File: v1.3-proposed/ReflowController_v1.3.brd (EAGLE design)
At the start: 95.2 x 50.8 mm, 53 parts, among them J1 AVR_SPI_PRG_62X3_LOCK

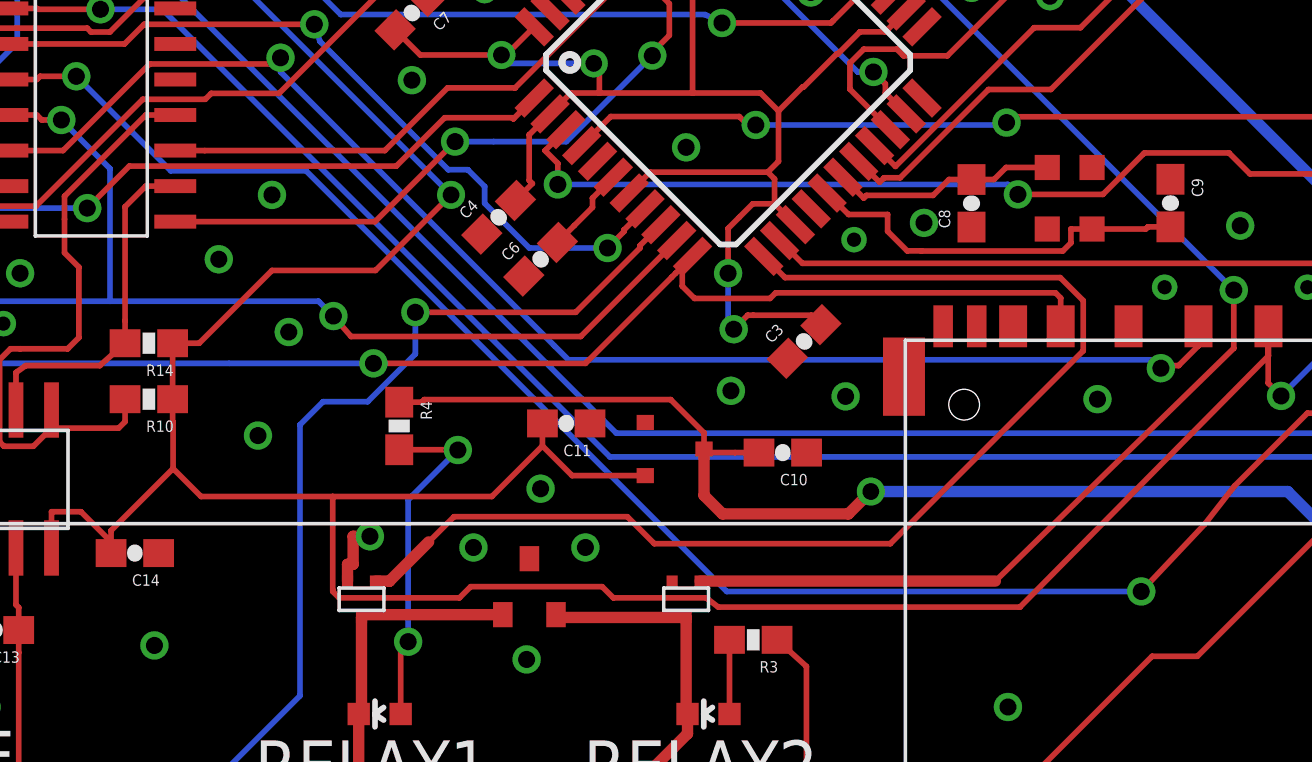
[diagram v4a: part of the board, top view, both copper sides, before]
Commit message: 16x2 LCD support, self test added, optimizations
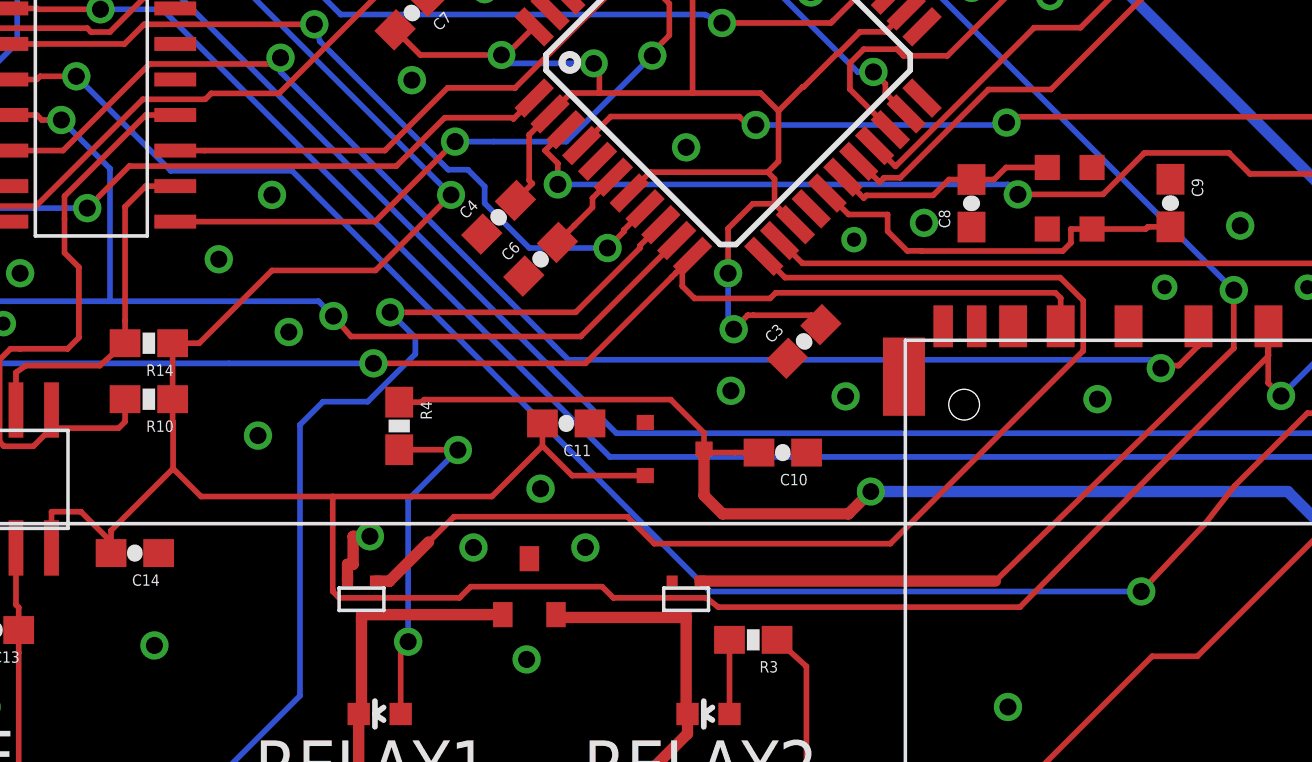
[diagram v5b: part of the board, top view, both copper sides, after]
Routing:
- net SCK: track 101.5 -> 102.8 mm
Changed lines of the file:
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@@
 <wire x1="10.1781" y1="14.9693" x2="10.1781" y2="13.7246" width="0.2032" layer="16"/>
 <wire x1="50.2978" y1="39.7354" x2="49.5519" y2="38.9895" width="0.2032" layer="1"/>
-<wire x1="41.5242" y1="36.6048" x2="47.2538" y2="36.6048" width="0.2032" layer="1"/>
+<wire x1="40.6242" y1="36.6048" x2="47.2538" y2="36.6048" width="0.2032" layer="1"/>
 <wire x1="47.2538" y1="36.6048" x2="49.5519" y2="38.9029" width="0.2032" layer="1"/>
 <wire x1="49.5519" y1="38.9029" x2="49.5519" y2="38.9895" width="0.2032" layer="1"/>
-<via x="41.5242" y="36.6048" extent="1-16" drill="0.609596875" diameter="1.016"/>
+<via x="40.6242" y="36.6048" extent="1-16" drill="0.609596875" diameter="1.016"/>
 <wire x1="10.1781" y1="13.7246" x2="10.956" y2="13.7246" width="0.2032" layer="16"/>
 <wire x1="10.956" y1="13.7246" x2="11.7021" y2="12.9785" width="0.2032" layer="16"/>
@@
 <wire x1="38.2256" y1="33.4099" x2="39.82" y2="33.4099" width="0.2032" layer="16"/>
 <wire x1="39.82" y1="33.4099" x2="41.5242" y2="35.1141" width="0.2032" layer="16"/>
-<wire x1="41.5242" y1="35.1141" x2="41.5242" y2="36.6048" width="0.2032" layer="16"/>
 <wire x1="10.1781" y1="14.9693" x2="10.1781" y2="16.214" width="0.2032" layer="1"/>
 <wire x1="26.944" y1="41.114" x2="25.8891" y2="41.114" width="0.2032" layer="1"/>
@@
 <wire x1="16.8" y1="19.7" x2="19.3" y2="22.2" width="0.2032" layer="1"/>
 <wire x1="50.2978" y1="39.7354" x2="50.297834375" y2="39.735421875" width="0" layer="19" extent="1-1"/>
+<wire x1="41.5242" y1="35.1141" x2="41.5242" y2="35.7048" width="0.2032" layer="16"/>
+<wire x1="41.5242" y1="35.7048" x2="40.6242" y2="36.6048" width="0.2032" layer="16"/>
 </signal>
 <signal name="SS">
@@
 <via x="67.4639" y="26.6288" extent="1-16" drill="0.609596875" diameter="1.016"/>
 <wire x1="29.4074" y1="45.0386" x2="32.7828" y2="41.6632" width="0.2032" layer="16"/>
-<wire x1="32.7828" y1="41.6632" x2="37.6157" y2="41.6632" width="0.2032" layer="16"/>
-<wire x1="37.6157" y1="41.6632" x2="52.6501" y2="26.6288" width="0.2032" layer="16"/>
-<wire x1="52.6501" y1="26.6288" x2="67.4639" y2="26.6288" width="0.2032" layer="16"/>
+<wire x1="32.7828" y1="41.6632" x2="37.1157" y2="41.6632" width="0.2032" layer="16"/>
+<wire x1="37.1157" y1="41.6632" x2="52.0501" y2="26.6288" width="0.2032" layer="16"/>
+<wire x1="52.0501" y1="26.6288" x2="67.4639" y2="26.6288" width="0.2032" layer="16"/>
 <via x="29.4074" y="45.0386" extent="1-16" drill="0.609596875" diameter="1.016"/>
 <wire x1="27.9989" y1="44.924" x2="28.1135" y2="45.0386" width="0.2032" layer="1"/>
